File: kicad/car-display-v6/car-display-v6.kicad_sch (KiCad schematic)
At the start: 38 parts, among them J1 AVR-ISP-10, J2 Screw_Terminal_01x03, J3 PicoBlade F 1x7, J4 Socket 1x6 0.1", J5 JMP 1x3 0.05", U1 ATmega328PB-M, U2 MCP25625T-E/ML, U3 TPSM365R1FRDNR, U4 TPSM365R15RDNR, Y1 16MHZ

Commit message: Work on V6 pCB
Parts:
- U3: value TPSM365R1FRDNR -> TPSM365R15FRDNR
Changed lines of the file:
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@@
 			)
 		)
-		(property "Value" "TPSM365R1FRDNR"
+		(property "Value" "TPSM365R15FRDNR"
 			(at 55.88 154.94 0)
 			(effects

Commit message: Work on V6 code for PlatformIO
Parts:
- removed C1: 2.2µF, Capacitor_SMD:C_0805_2012Metric, symbol Device:C
- removed C15, C2: 100nF, Capacitor_SMD:C_0402_1005Metric, symbol Device:C
- removed C3: 1µF, Capacitor_SMD:C_0603_1608Metric, symbol Device:C
- removed C4: 10µF, Capacitor_SMD:C_0805_2012Metric, symbol Device:C
- removed FB1, FB2: FerriteBead_Small_Array, jsdev:fb_array_0805, symbol jsdev:FerriteBead_Small_Array
- removed U2: MCP25625T-E/ML, jsdev:QFN-28-1EP_6x6mm_P0.65mm_EP4.25x4.25mm_mod1, symbol jsdev:MCP25625T-E/ML
- removed U3: TPSM365R15FRDNR, jsdev:QFN-FCMOD_TI_11B, symbol jsdev:TPSM365R1x
- added C12: 100nF, Capacitor_SMD:C_0402_1005Metric, symbol Device:C
- added FB1, FB2, FB3, FB4, FB5, FB6, FB7: 120X, Inductor_SMD:L_0402_1005Metric, symbol Device:FerriteBead_Small
- added H3: MountingHole_Pad, MountingHole:MountingHole_2.2mm_M2_DIN965, symbol Mechanical:MountingHole
- added U2: MCP2515-xST, Package_SO:TSSOP-20_4.4x6.5mm_P0.65mm, symbol Interface_CAN_LIN:MCP2515-xST
- added U3: TCAN332, jsdev:SOT-23-8-MOD, symbol Interface_CAN_LIN:TCAN332
- C1: renamed from C17; value C_Polarized -> 100uF
- renumbered C13 to C10, C14 to C11, C16 to C13, C9 to C2, C5 to C3, C6 to C4, C7 to C5, C8 to C6, C10 to C7, C11 to C8, C12 to C9, R6 to R1, R5 to R2, R8 to R3, R7 to R4
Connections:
- net +5V is gone; now on net +3.3V: C13.1
- net +3.3V: now also C12.1, FB7.2, U2.20 (VDD), U3.3 (VCC)
- net 3F_3.3V: now also FB7.1
- net 3F_CS_OLED: now also FB5.1
- net 3F_GND: now also FB6.1
- net 3F_MOSI: now also FB1.1
- net 3F_OLED_DC: now also FB3.1
- net 3F_OLED_RST: now also FB4.1
- net 3F_SCK: now also FB2.1
- net CANH: now also U3.7 (CANH)
- net CAN_CLK_PD: now also U2.8 (OSC2)
- net CLK: now also U2.9 (OSC1)
- net CS_CAN: now also U2.18 (~{CS})
- net CS_OLED: now also FB5.2
- net DC_OLED: now also FB3.2
- net GND: now also C12.2, FB6.2, U2.10 (VSS), U3.2 (GND), U3.6 (CANL)
- net INT_CAN: now also U1.25 (PC2), U2.13 (~{INT}); no longer U1.11 (PD7)
- net MISO: now also U2.17 (SO)
- net MOSI: now also FB1.2, U2.16 (SI)
- net RESET: now also U2.19 (~{RESET})
- net RST_OLED: now also FB4.2
- net R_{X}CAN: now also U2.2 (RXCAN), U3.4 (RXD)
- net SCK: now also FB2.2, U2.14 (SCK)
- net SEL_UNIT: now also U1.26 (PC3); no longer U1.25 (PC2)
- net T_{X}CAN: now also U2.1 (TXCAN), U3.1 (TXD)
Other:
- note added: "1"
- note added: "1,19,27"
- note added: "10"
- note added: "11"
- note added: "12"
- note added: "13"
- note added: "14"
- note added: "15"
- note added: "18"
- note added: "19"
- note added: "2"
- note added: "20"
- note added: "21"
- note added: "23"
- note added: "24"
- note added: "25"
- note added: "26"
- note added: "27"
- note added: "28"
- note added: "3"
- note added: "5"
- note added: "6"
- note added: "8,22"
- note added: "9"
- note added: "Blue text for Arduino Uno pins"
- note added: "POWER SUPPLY"
- note added: "Red text for ATMEGA328PB QFN"
- note added: "Red text for MCP2515 QFN"
- note added: "Violet text for ATMEGA328P DIP"
- note added: "Violet text for MCP25625 SSOP"
- note removed: "POWER SUPPLIES"
- moved on the sheet: C13, C3, C4, C5, C6, C7, C8, C9, D2, R1, R3, U4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

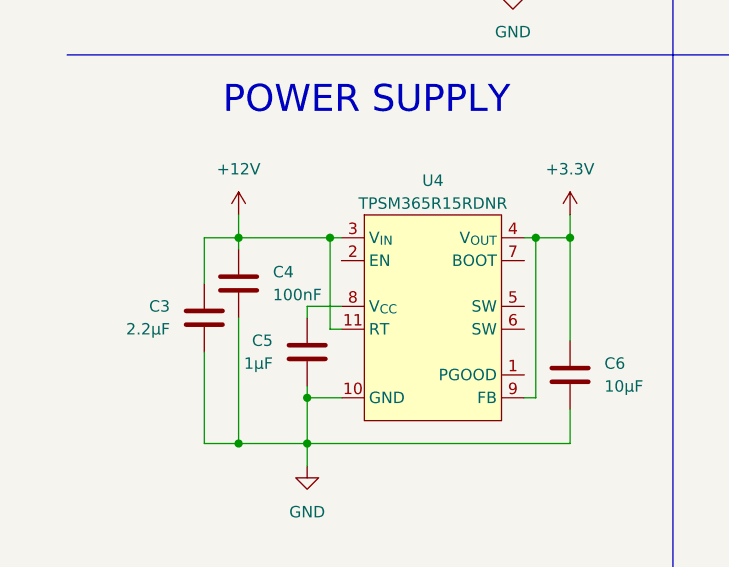
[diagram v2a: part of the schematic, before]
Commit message: Fix PSU error
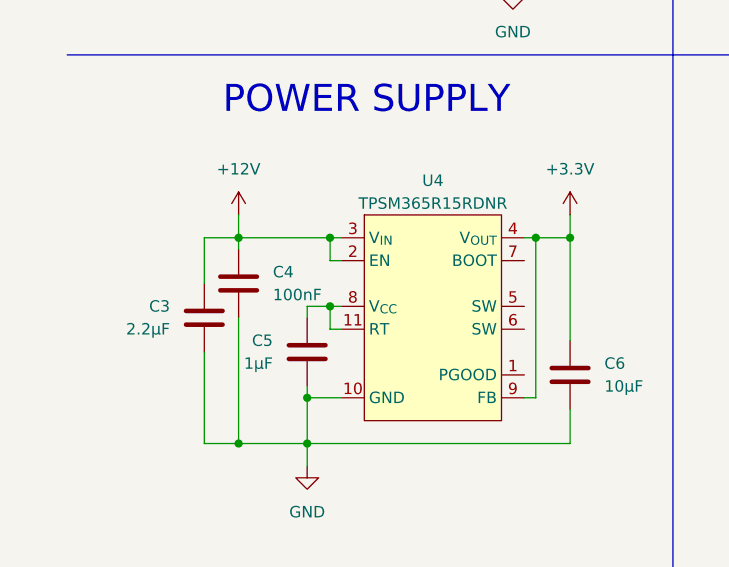
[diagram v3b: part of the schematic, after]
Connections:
- net +12V: now also U4.2 (EN); no longer U4.11 (RT)
- net at C5.1, U4.8 (V_{CC}): now also U4.11 (RT)
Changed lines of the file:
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@@
+	)
+	(junction
+		(at 41.91 162.56)
+		(diameter 0)
+		(color 0 0 0 0)
 	)
 	(junction
@@
 	(wire
 		(pts
-			(xy 41.91 154.94) (xy 41.91 165.1)
+			(xy 41.91 154.94) (xy 41.91 157.48)
 		)
 		(stroke
@@
 		)
 	)
+	(wire
+		(pts
+			(xy 41.91 157.48) (xy 43.18 157.48)
+		)
+		(stroke
+			(width 0)
+			(type default)
+		)
+	)
 	(polyline
 		(pts
@@
 	(wire
 		(pts
+			(xy 41.91 162.56) (xy 41.91 165.1)
+		)
+		(stroke
+			(width 0)
+			(type default)
+		)
+	)
+	(wire
+		(pts
 			(xy 245.11 121.92) (xy 231.14 121.92)
 		)
@@
 	(wire
 		(pts
+			(xy 41.91 162.56) (xy 39.37 162.56)
+		)
+		(stroke
+			(width 0)
+			(type default)
+		)
+	)
+	(wire
+		(pts
 			(xy 69.85 115.57) (xy 72.39 115.57)
 		)
@@
 	(wire
 		(pts
-			(xy 43.18 162.56) (xy 39.37 162.56)
-		)
-		(stroke
+			(xy 43.18 162.56) (xy 41.91 162.56)
+		)
+		(stroke

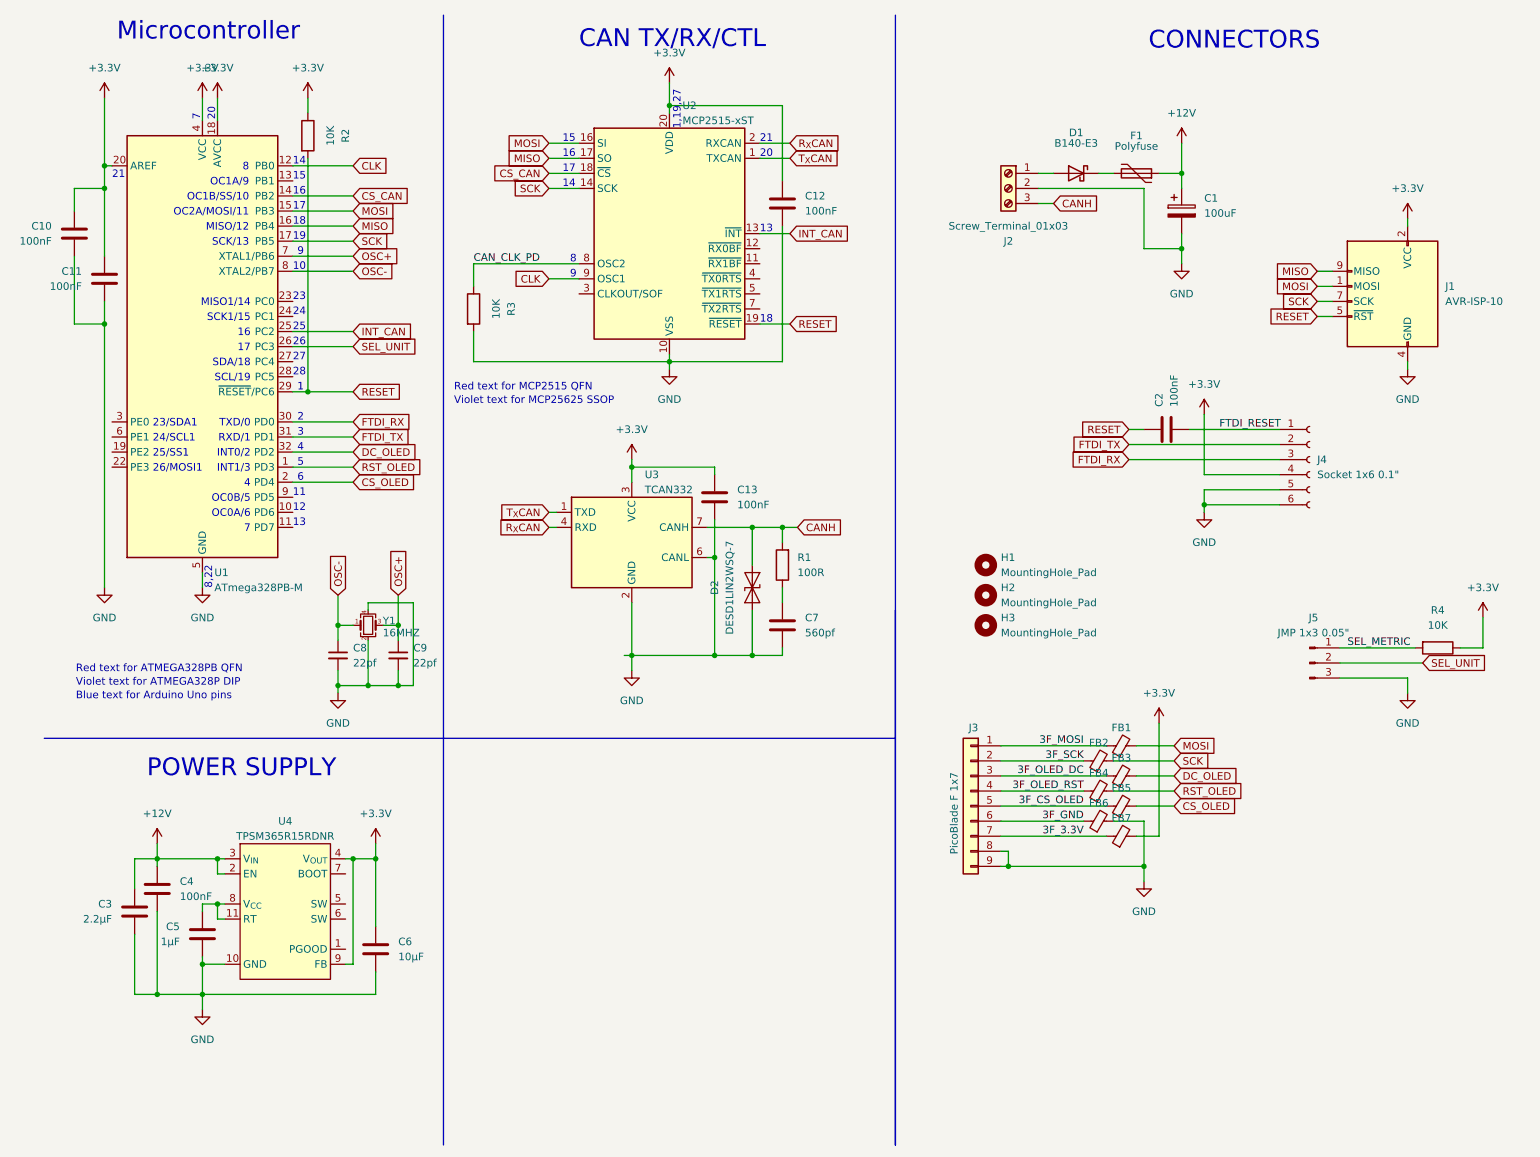
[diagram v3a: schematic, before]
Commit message: Update PCB with new power supply and return to MCP25625
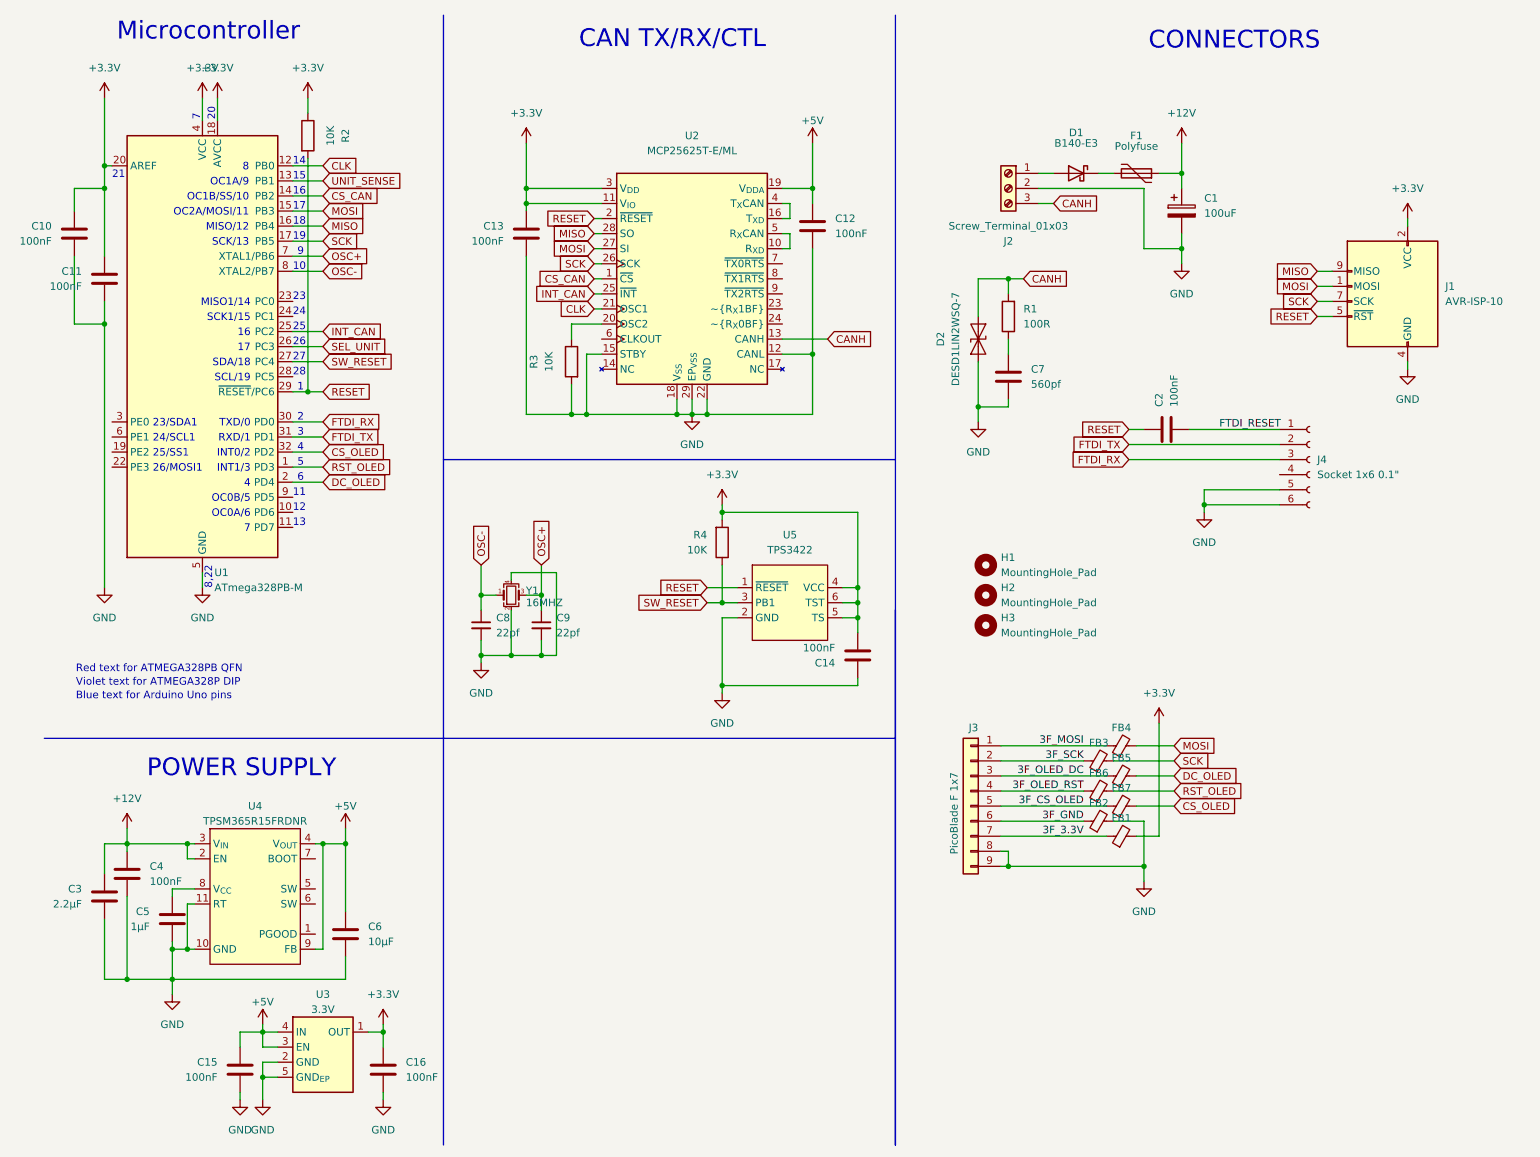
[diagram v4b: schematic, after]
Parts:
- removed J5: JMP 1x3 0.05", jsdev:PinHeader_1x03_P1.27mm_Vertical_mod, symbol Connector:Conn_01x03_Pin
- removed U2: MCP2515-xST, Package_SO:TSSOP-20_4.4x6.5mm_P0.65mm, symbol Interface_CAN_LIN:MCP2515-xST
- removed U3: TCAN332, jsdev:SOT-23-8-MOD, symbol Interface_CAN_LIN:TCAN332
- added C14, C15, C16: 100nF, Capacitor_SMD:C_0402_1005Metric, symbol Device:C
- added U2: MCP25625T-E/ML, Package_DFN_QFN:QFN-28-1EP_6x6mm_P0.65mm_EP4.25x4.25mm, symbol jsdev:MCP25625T-E/ML
- added U3: 3.3V, jsdev:Texas_X2SON-4_1x1mm_P0.65mm_MOD, symbol jsdev:TLV713-4XDFNEP
- added U5: TPS3422, Package_SON:Texas_USON-6_1x1.45mm_P0.5mm_SMD, symbol jsdev:TPS3422
- J1: footprint jsdev:PinHeader_ISP10_POGO -> jsdev:PinHeader_SWD_BD120-10-A-0305-0229-L-B
- U4: value TPSM365R15RDNR -> TPSM365R15FRDNR
- renumbered FB7 to FB1, FB6 to FB2, FB2 to FB3, FB1 to FB4, FB3 to FB5, FB4 to FB6, FB5 to FB7
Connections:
- net SEL_METRIC is gone; now on net +3.3V: R4.2
- net +3.3V: now also C14.2, C16.1, U2.11 (V_{IO}), U2.3 (V_{DD}), U3.1 (OUT), U5.4 (VCC), U5.5 (TS), U5.6 (TST); no longer C12.1, C6.1, J4.4 (Pin_4), R4.1, U4.4 (V_{OUT}), U4.9 (FB)
- net CANH: now also U2.13 (CANH)
- net CLK: now also U2.21 (OSC1)
- net CS_CAN: now also U2.1 (~{CS})
- net CS_OLED: now also U1.32 (PD2); no longer U1.2 (PD4)
- net DC_OLED: now also U1.2 (PD4); no longer U1.32 (PD2)
- net GND: now also U4.11 (RT), C14.1, C15.2, C16.2, U2.12 (CANL), U2.15 (STBY), U2.18 (V_{SS}), U2.22 (GND), U2.29 (EP_{VSS}), U3.2 (GND), U3.5 (GND_{EP}), U5.2 (GND)
- net INT_CAN: now also U2.25 (~{INT})
- net MISO: now also U2.28 (SO)
- net MOSI: now also U2.27 (SI)
- net RESET: now also U2.2 (~{RESET}), U5.1 (~{RESET})
- net SCK: now also U2.26 (SCK)
- net at C5.1, U4.8 (V_{CC}): no longer U4.11 (RT)
- net UNIT_SENSE: now reaches U1.13 (PB1)
- net SW_RESET: now reaches U1.27 (PC4)
- net SW_RESET: now also R4.1, U5.3 (PB1)
- net CAN_CLK_PD: no longer names the net of R3.1
- net CAN_CLK_PD: now also U2.20 (OSC2)
- new net: U2.10 (R_{XD}), U2.5 (R_{X}CAN)
- new net: U2.16 (T_{XD}), U2.4 (T_{X}CAN)
- new net +5V: C12.1, C15.1, C6.1, U2.19 (V_{DDA}), U3.3 (EN), U3.4 (IN), U4.4 (V_{OUT}), U4.9 (FB)
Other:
- note removed: "1,19,27"
- note removed: "Red text for MCP2515 QFN"
- note removed: "Violet text for MCP25625 SSOP"
- moved on the sheet: C3, C4, C5, C6, C7, C8, C9, D2, R1, U4, Y1
